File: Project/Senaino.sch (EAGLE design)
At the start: 34 parts, among them Q1 16 MHz, U1 ATMEGA328P-PU, U2 FT232RL, U3 7805T, X1 POWERSUPPLY_DC21MMX

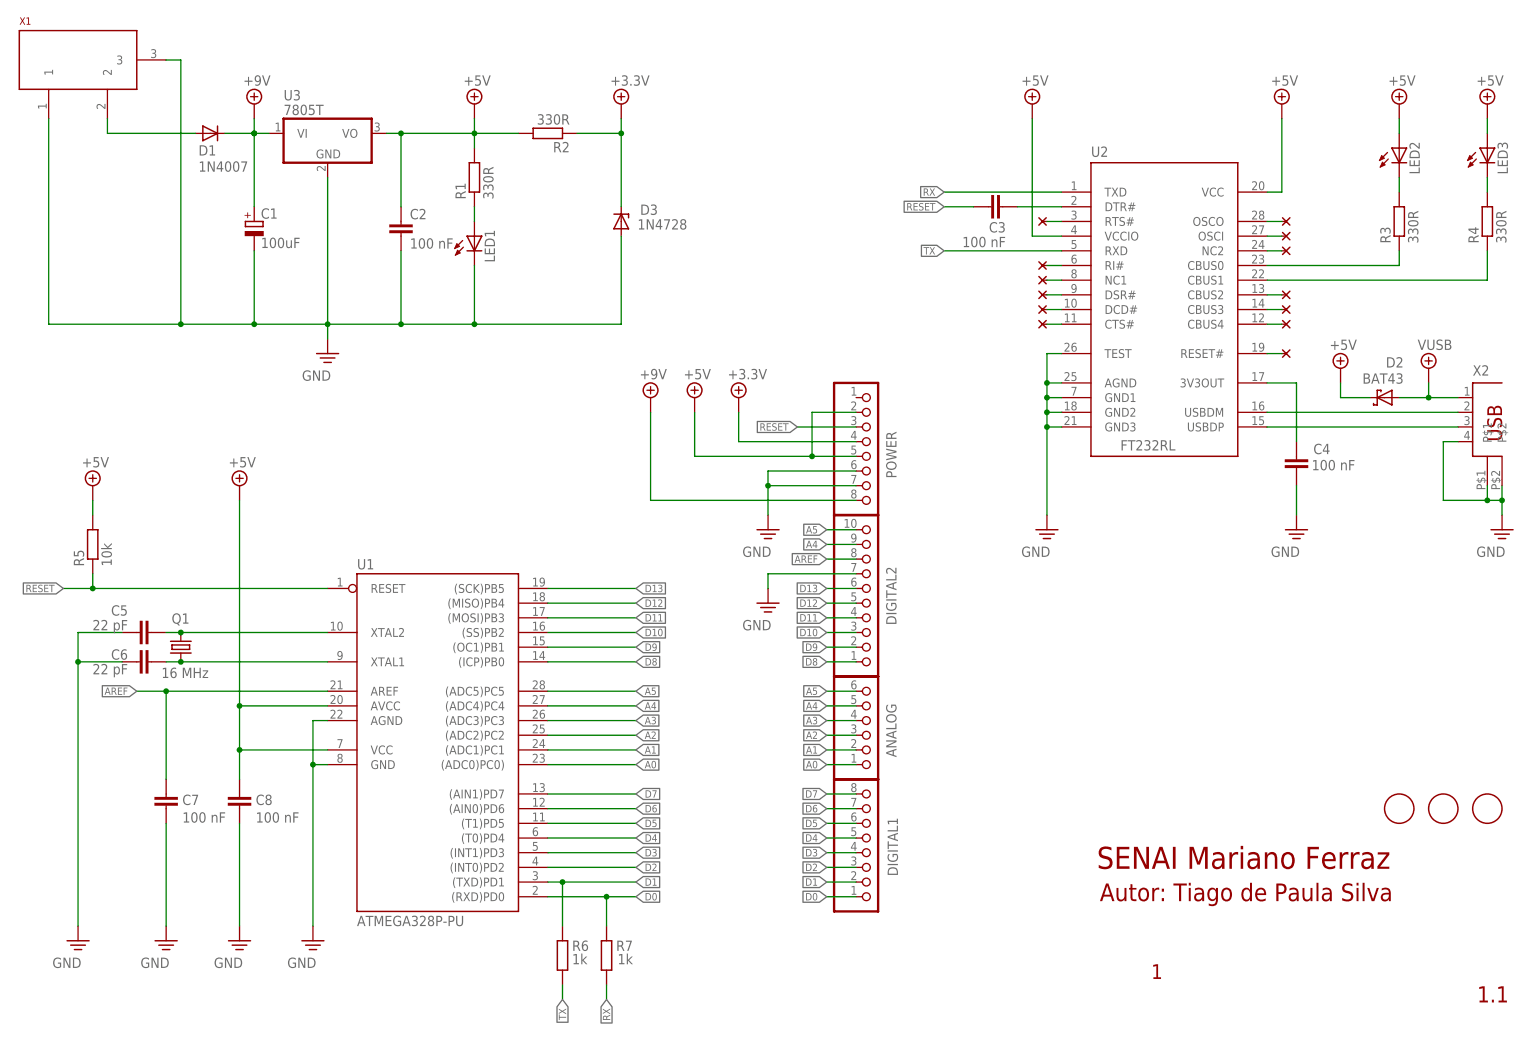
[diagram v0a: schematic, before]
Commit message: USB/Serial Converter Chip Change
- The FT232 USB/Serial converter changed by CH340.

- The reason for this is to create a second alternative to FT232 converter. This is not always available in large quantities in the Brazilian market.

- In addition, CH340 encapsulation is easier to solder on the board.
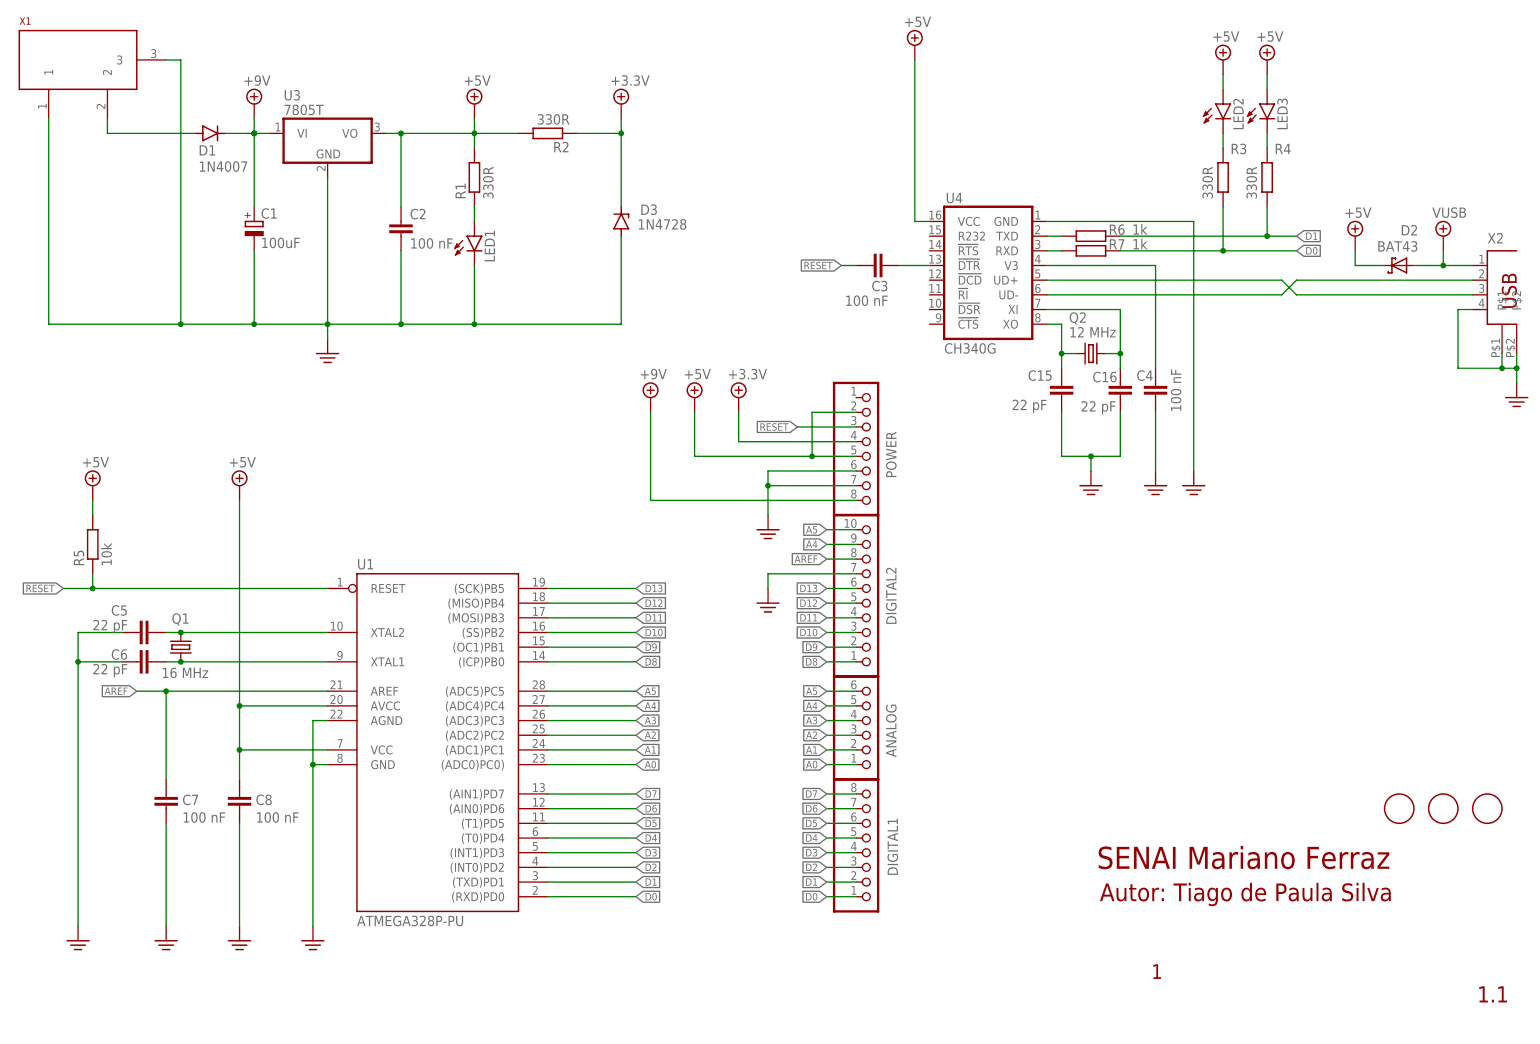
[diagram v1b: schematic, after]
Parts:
- removed U2: FT232RL, MySMD2:FT232RL
- added C15, C16: 22 pF, rcl:C-EU025-024X044
- added Q2: 12 MHz, crystal:CRYSTALHC49S
- added U4: CH340G, Serial-Basic:CH340GSMD
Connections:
- removed net N$14: U2.NC1
- removed net N$15: U2.DSR#
- removed net N$16: U2.DCD#
- removed net N$17: U2.OSCO
- removed net N$18: U2.OSCI
- removed net N$19: U2.NC2
- removed net N$20: U2.CBUS2
- removed net N$21: U2.CBUS3
- removed net N$22: U2.CBUS4
- removed net N$23: U2.RESET#
- removed net N$27: U2.RTS#
- removed net RX: R7.1, U2.TXD
- removed net TX: R6.1, U2.RXD
- new net PE: C15.1, C16.1, U4.GND
- net +5V: now also U4.VCC; no longer U2.VCC, U2.VCCIO
- net D0: now also R3.1
- net D1: now also R4.1
- net GND: no longer U2.AGND, U2.GND1, U2.GND2, U2.GND3, U2.TEST
- net N$10: now also R7.1, U4.RXD; no longer R4.1, U2.CBUS1
- net N$11: now also U4.V3; no longer U2.3V3OUT
- net N$12: now also C15.2, Q2.2, U4.XO; no longer U2.CTS#
- net N$13: now also C16.2, Q2.1, U4.XI; no longer U2.RI#
- net N$2: now also U4.UD+, X2.3; no longer U2.USBDM, X2.2
- net N$3: now also U4.!DTR; no longer U2.DTR#
- net N$4: now also R6.1, U4.TXD; no longer R3.1, U2.CBUS0
- net N$5: now also U4.UD-, X2.2; no longer U2.USBDP, X2.3
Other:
- moved on the sheet: C3, C4, D2, R3, R4, R6, R7, X2
